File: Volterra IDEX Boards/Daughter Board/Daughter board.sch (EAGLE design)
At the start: 53 parts, among them J14 FEMALE 2x3, J5 455-1750-1-ND, J6 455-1750-1-ND, J7 455-1750-1-ND, K1 FFC/FPC/34PIN/1MMPITCH/TOPLOCK, X10 FIL_HEAT, X11 FIL_THM, X12 CH_THM, X13 CH_HEAT, X14 24V, X2 EXTDR-0, X3 EXTDR-1, X4 Z_LMT, X5 BED_THERM, X6 24V, X7 24V, X8 AUTO BED LEVELING, X9 Y_LMT

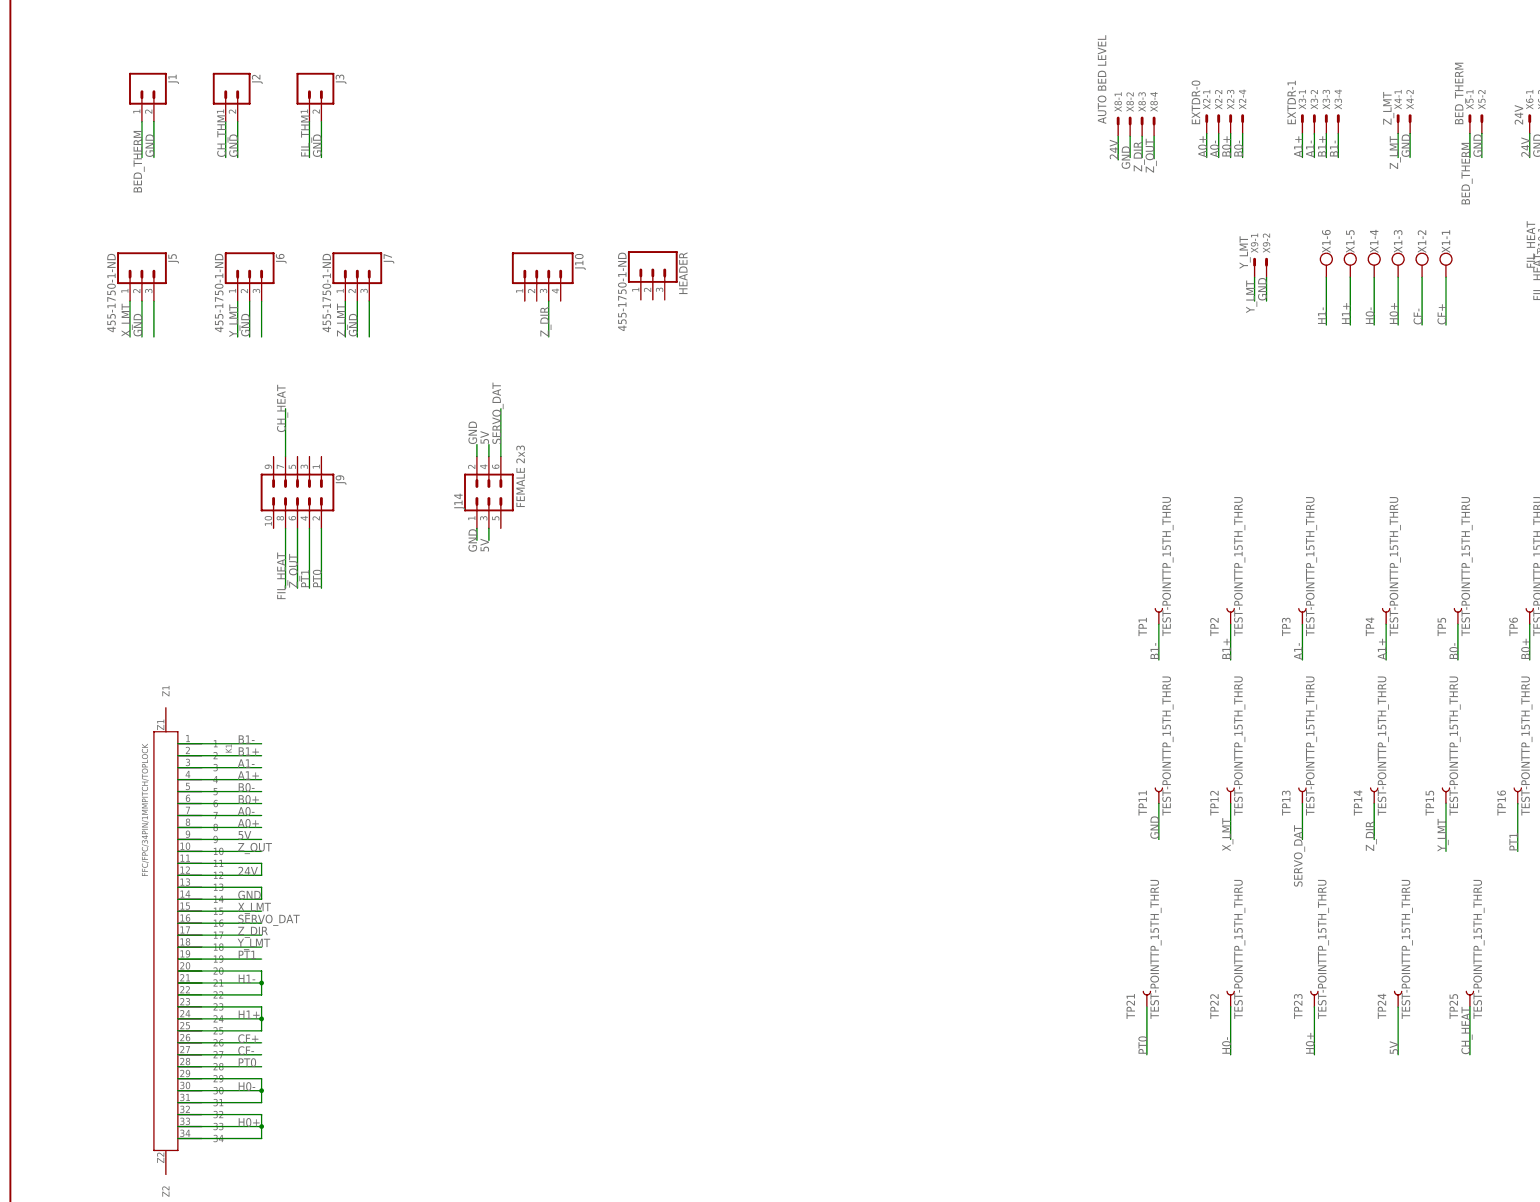
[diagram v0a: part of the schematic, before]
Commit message: Updated Daughter board schematic and other boards
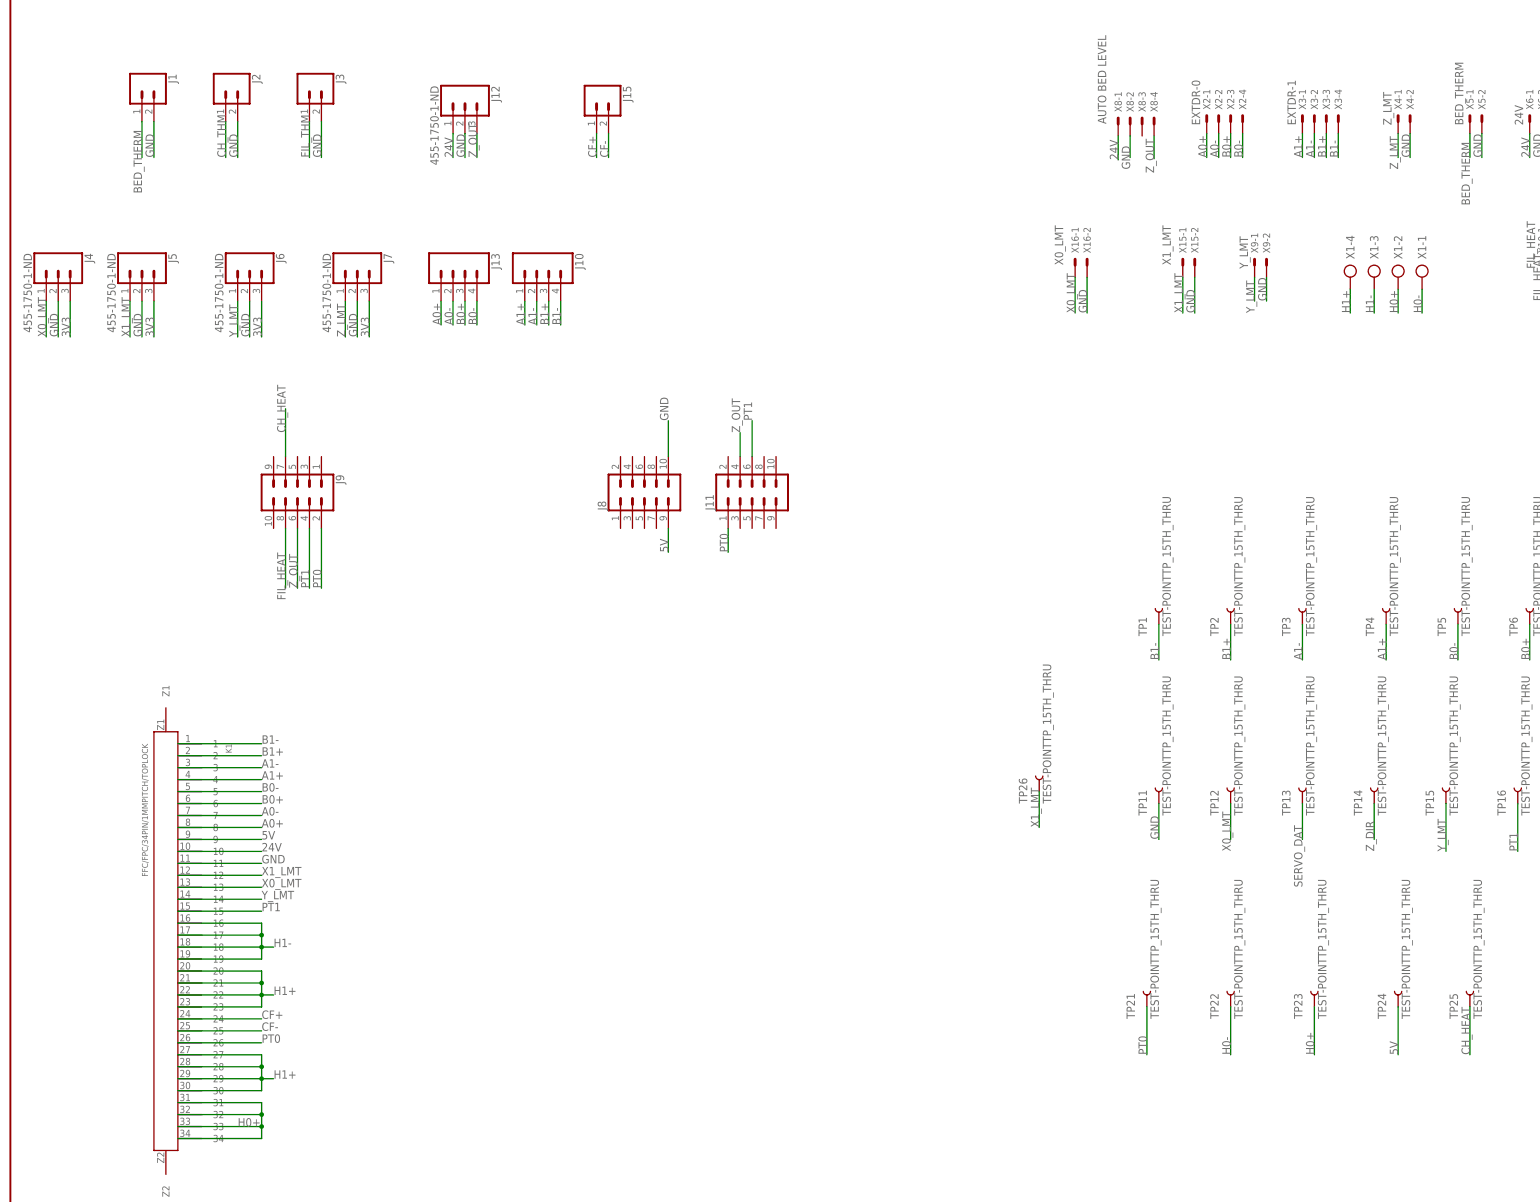
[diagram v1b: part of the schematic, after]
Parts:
- removed HEADER: 455-1750-1-ND, SparkFun-Connectors:CONN_03
- removed J14: FEMALE 2x3, SparkFun-Connectors:CONN_03X2FEMALE
- added J11, J8: (no value), SparkFun-Connectors:CONN_05X2NO_SILK
- added J12, J4: 455-1750-1-ND, SparkFun-Connectors:CONN_03
- added J13: (no value), SparkFun-Connectors:CONN_04
- added J15: (no value), SparkFun-Connectors:CONN_02
- added TP26: TEST-POINTTP_15TH_THRU, SparkFun-Connectors:TEST-POINTTP_15TH_THRU
- added X15, X16: JST-XH-02-PIN-LONG-PAD, Rembrandt Electronics - JST XH Connectors v1-0:JST-XH-02-PIN-LONG-PAD
- X1: device con-wago-500:W237-6 -> con-ptr500:AK500/4
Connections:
- removed net N$10: J7.3
- removed net N$3: J5.3
- removed net N$6: J6.3
- removed net X_LMT: J5.1, K1.15, TP12.1
- new net 3V3: J4.3, J5.3, J6.3, J7.3
- new net X0_LMT: J4.1, K1.13, TP12.1, X16-1.S
- new net X1_LMT: J5.1, K1.12, TP26.1, X15-1.S
- net 24V: now also J12.1, K1.10; no longer K1.11, K1.12
- net 5V: now also J8.9; no longer J14.3, J14.4
- net A0+: now also J13.1
- net A0-: now also J13.2
- net A1+: now also J10.1
- net A1-: now also J10.2
- net B0+: now also J13.3
- net B0-: now also J13.4
- net B1+: now also J10.3
- net B1-: now also J10.4
- net CF+: now also J15.1, K1.24; no longer K1.26, X1-1.KL
- net CF-: now also J15.2, K1.25; no longer K1.27, X1-2.KL
- net GND: now also J12.2, J4.2, J8.10, K1.11, X15-2.S, X16-2.S; no longer J14.1, J14.2, K1.13, K1.14
- net H0+: now also K1.31, X1-2.KL; no longer X1-3.KL
- net H0-: now also X1-1.KL; no longer K1.29, K1.30, K1.31, X1-4.KL
- net H1+: now also K1.20, K1.21, K1.22, K1.27, K1.28, K1.29, K1.30, X1-4.KL; no longer K1.24, K1.25, X1-5.KL
- net H1-: now also K1.16, K1.17, K1.18, K1.19, X1-3.KL; no longer K1.20, K1.21, K1.22, X1-6.KL
- net PT0: now also J11.1, K1.26; no longer K1.28
- net PT1: now also J11.6, K1.15; no longer K1.19
- net SERVO_DAT: no longer J14.6, K1.16
- net Y_LMT: now also K1.14; no longer K1.18
- net Z_DIR: no longer J10.3, K1.17, X8-3.S
- net Z_OUT: now also J11.4, J12.3; no longer K1.10
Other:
- moved on the sheet: X1-1, X1-2, X1-3, X1-4

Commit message: Added Daughter Board
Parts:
- removed J13: (no value), SparkFun-Connectors:CONN_04
- removed J8: (no value), SparkFun-Connectors:CONN_05X2NO_SILK
- removed J9: (no value), SparkFun-Connectors:CONN_05X2PTH
- removed TP13, TP14, TP25: TEST-POINTTP_15TH_THRU, SparkFun-Connectors:TEST-POINTTP_15TH_THRU
- removed X10: FIL_HEAT, Rembrandt Electronics - JST XH Connectors v1-0:JST-XH-02-PIN-LONG-PAD
- removed X13: CH_HEAT, Rembrandt Electronics - JST XH Connectors v1-0:JST-XH-02-PIN-LONG-PAD
- removed X14: 24V, Rembrandt Electronics - JST XH Connectors v1-0:JST-XH-02-PIN-LONG-PAD
- removed X15, X16: JST-XH-02-PIN-LONG-PAD, Rembrandt Electronics - JST XH Connectors v1-0:JST-XH-02-PIN-LONG-PAD
- J10: device SparkFun-Connectors:CONN_04 -> SparkFun-Connectors:CONN_02
- J12: value 455-1750-1-ND -> RGB LED
- X9: value Y_LMT -> RGB LED; device Rembrandt Electronics - JST XH Connectors v1-0:JST-XH-02-PIN-LONG-PAD -> Rembrandt Electronics - JST XH Connectors v1-0:JST-XH-03-PIN-LONG-PAD
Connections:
- removed net CH_HEAT: J9.7, TP25.1, X13-1.S
- removed net FIL_HEAT: J9.8, X10-1.S
- removed net SERVO_DAT: TP13.1
- removed net Z_DIR: TP14.1
- new net PB0: J12.2, X9-2.S
- net 24V: now also J10.1, J10.2; no longer J12.1, X14-1.S
- net 5V: now also J12.3, X9-3.S; no longer J8.9
- net A0+: no longer J13.1
- net A0-: no longer J13.2
- net A1+: no longer J10.1
- net A1-: no longer J10.2
- net B0+: no longer J13.3
- net B0-: no longer J13.4
- net B1+: no longer J10.3
- net B1-: no longer J10.4
- net GND: now also J12.1, X9-1.S; no longer J12.2, J8.10, X10-2.S, X13-2.S, X14-2.S, X15-2.S, X16-2.S, X9-2.S
- net H0-: now also K1.27, K1.28, K1.29, K1.30
- net H1+: no longer K1.27, K1.28, K1.29, K1.30
- net PT0: no longer J9.2
- net PT1: no longer J9.4
- net X0_LMT: no longer X16-1.S
- net X1_LMT: no longer X15-1.S
- net Y_LMT: no longer X9-1.S
- net Z_OUT: now also J11.3; no longer J11.4, J12.3, J9.6
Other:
- moved on the sheet: J11, TP1, TP10, TP2, TP3, TP4, TP5, TP6, TP7, TP8, TP9, X9-1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
